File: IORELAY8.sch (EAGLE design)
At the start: 54 parts, among them J1 M08-SCREW-3.5MM, J2 M08-SCREW-3.5MM, J3 M10-PLAIN, J4 M06X2-SHROUDED, Q1 2N7002, Q2 2N7002, Q3 2N7002, Q4 2N7002, Q5 2N7002, Q6 2N7002, Q7 2N7002, Q8 2N7002

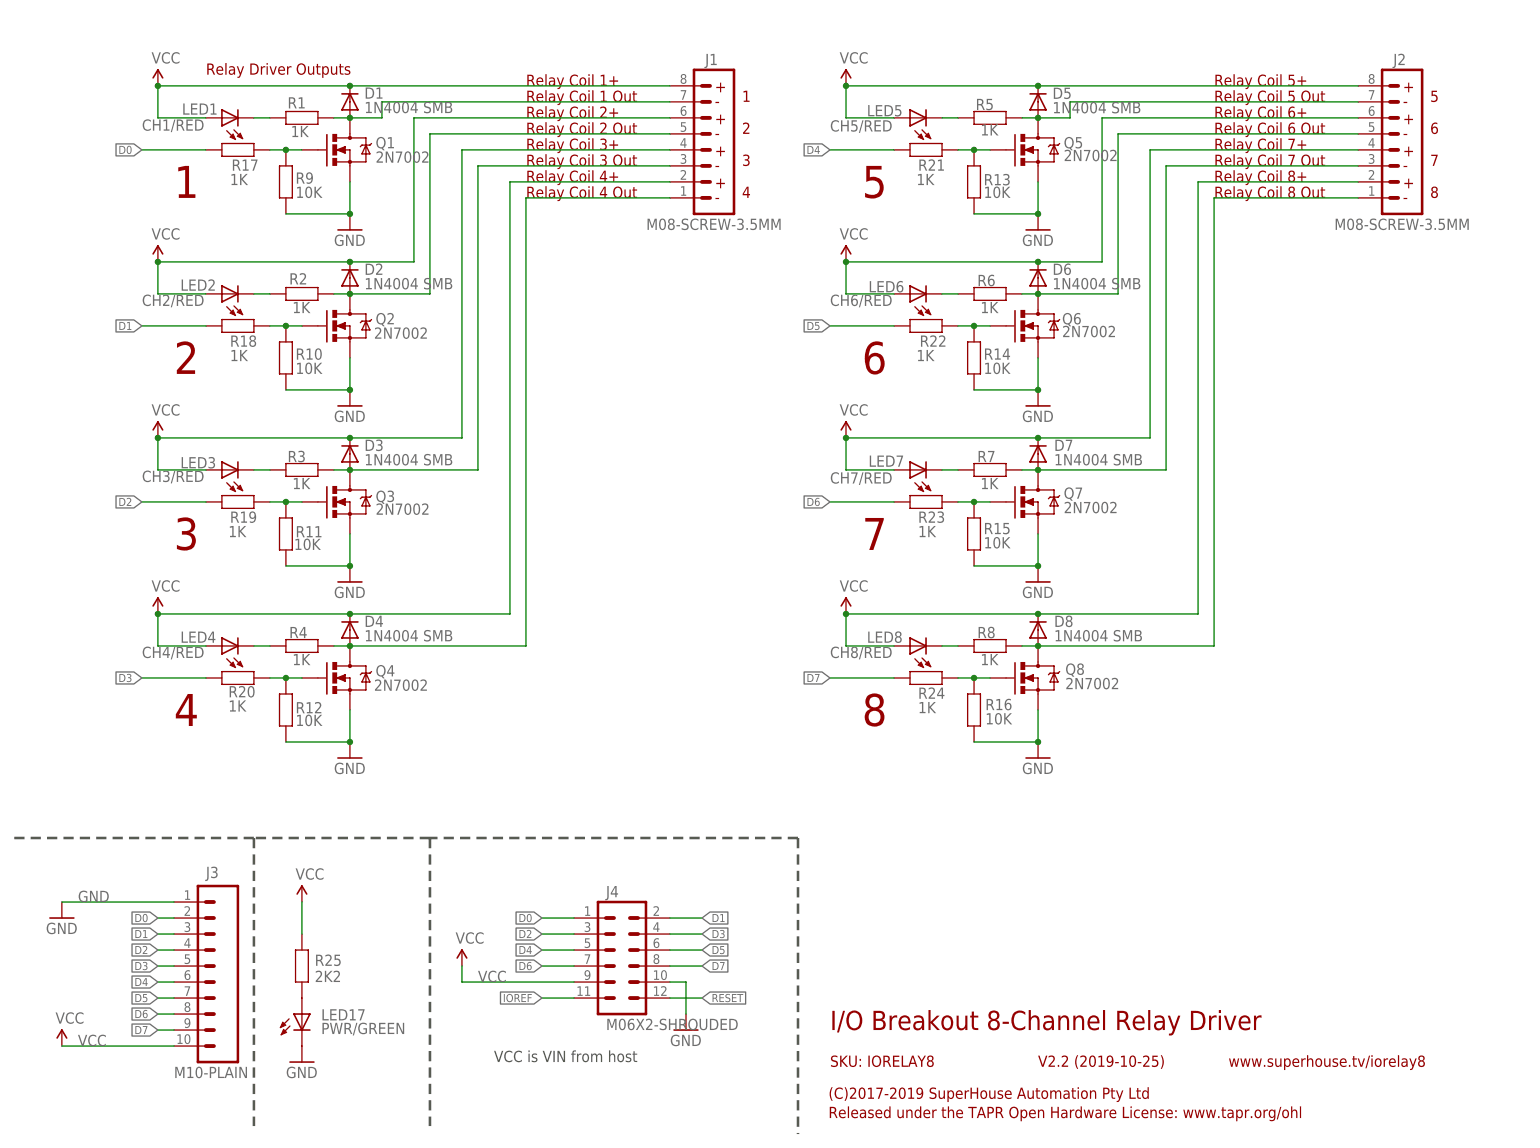
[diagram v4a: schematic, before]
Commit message: DRC, designator, and value cleanups for v2.2 release
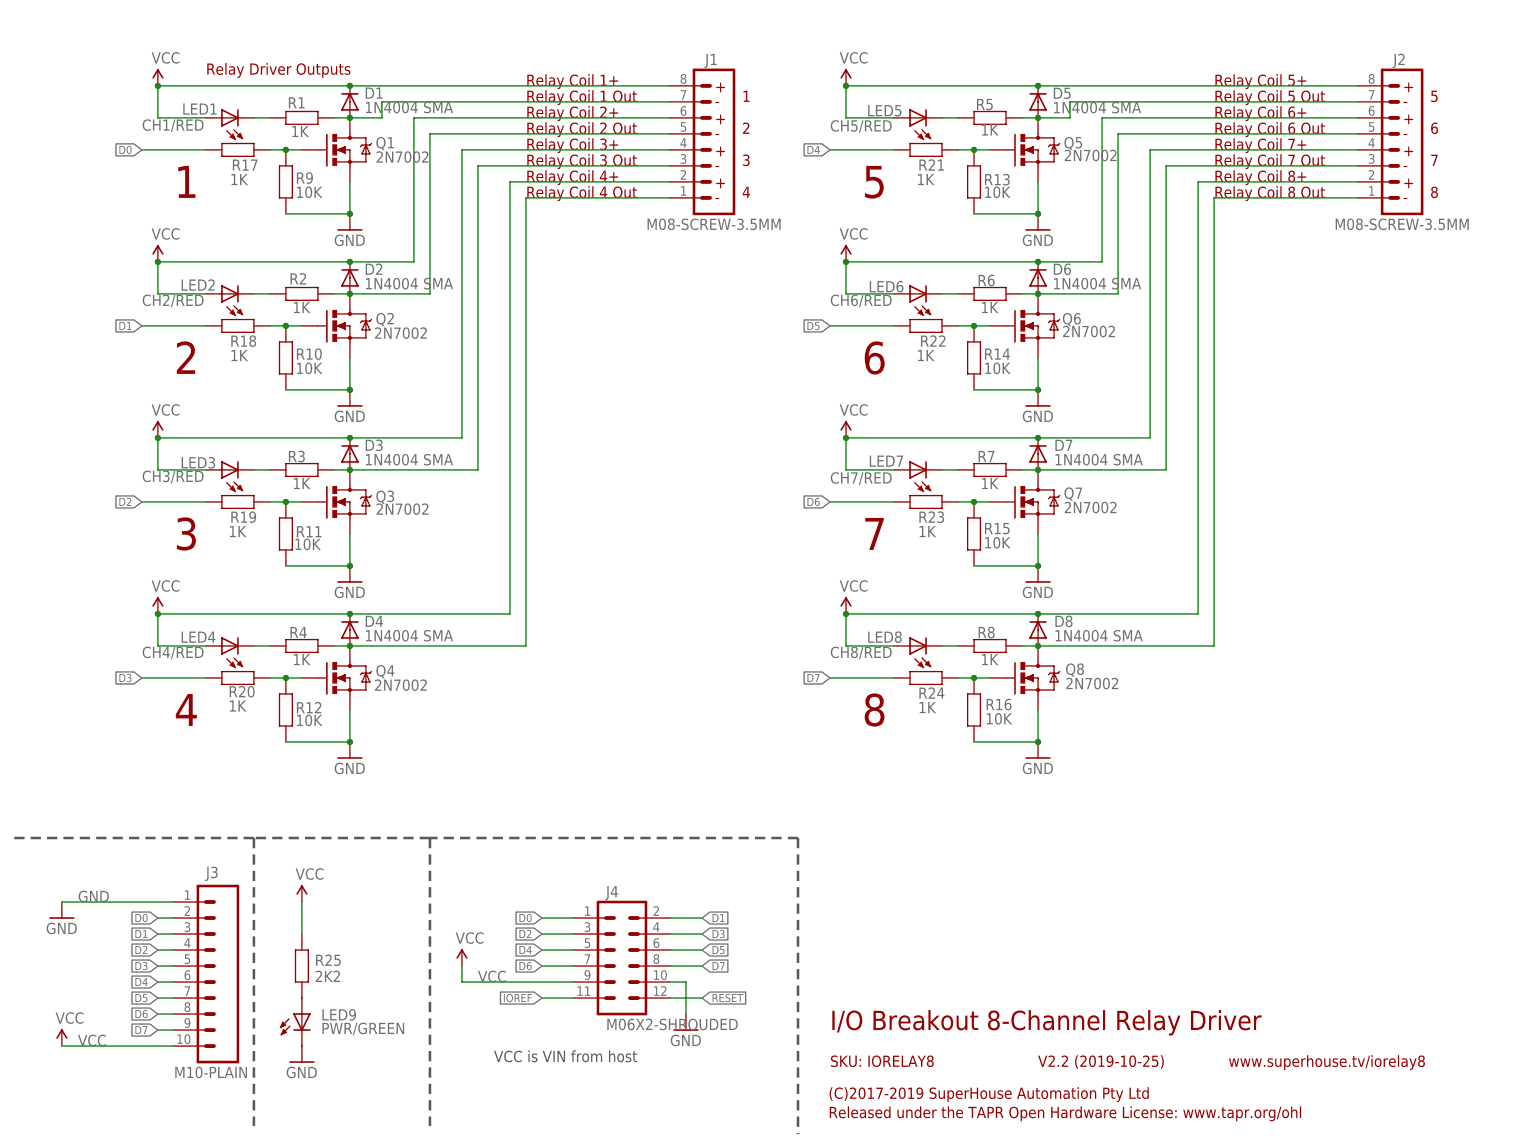
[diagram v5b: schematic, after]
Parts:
- D1, D2, D3, D4, D5, D6, D7, D8: value 1N4004 SMB -> 1N4004 SMA
- renumbered LED17 to LED9
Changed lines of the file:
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@@
 <part name="R7" library="SuperHouse-DiscreteSemi" library_urn="urn:adsk.eagle:library:11768461" deviceset="RESISTOR" device="0603" package3d_urn="urn:adsk.eagle:package:11768543/2" value="1K"/>
 <part name="R8" library="SuperHouse-DiscreteSemi" library_urn="urn:adsk.eagle:library:11768461" deviceset="RESISTOR" device="0603" package3d_urn="urn:adsk.eagle:package:11768543/2" value="1K"/>
-<part name="D1" library="SuperHouse-DiscreteSemi" library_urn="urn:adsk.eagle:library:11768461" deviceset="DIODE" device="SMA" package3d_urn="urn:adsk.eagle:package:7066222/3" value="1N4004 SMB"/>
-<part name="D2" library="SuperHouse-DiscreteSemi" library_urn="urn:adsk.eagle:library:11768461" deviceset="DIODE" device="SMA" package3d_urn="urn:adsk.eagle:package:7066222/3" value="1N4004 SMB"/>
-<part name="D3" library="SuperHouse-DiscreteSemi" library_urn="urn:adsk.eagle:library:11768461" deviceset="DIODE" device="SMA" package3d_urn="urn:adsk.eagle:package:7066222/3" value="1N4004 SMB"/>
-<part name="D4" library="SuperHouse-DiscreteSemi" library_urn="urn:adsk.eagle:library:11768461" deviceset="DIODE" device="SMA" package3d_urn="urn:adsk.eagle:package:7066222/3" value="1N4004 SMB"/>
-<part name="D5" library="SuperHouse-DiscreteSemi" library_urn="urn:adsk.eagle:library:11768461" deviceset="DIODE" device="SMA" package3d_urn="urn:adsk.eagle:package:7066222/3" value="1N4004 SMB"/>
-<part name="D6" library="SuperHouse-DiscreteSemi" library_urn="urn:adsk.eagle:library:11768461" deviceset="DIODE" device="SMA" package3d_urn="urn:adsk.eagle:package:7066222/3" value="1N4004 SMB"/>
-<part name="D7" library="SuperHouse-DiscreteSemi" library_urn="urn:adsk.eagle:library:11768461" deviceset="DIODE" device="SMA" package3d_urn="urn:adsk.eagle:package:7066222/3" value="1N4004 SMB"/>
-<part name="D8" library="SuperHouse-DiscreteSemi" library_urn="urn:adsk.eagle:library:11768461" deviceset="DIODE" device="SMA" package3d_urn="urn:adsk.eagle:package:7066222/3" value="1N4004 SMB"/>
-<part name="LED17" library="SuperHouse-LEDs" library_urn="urn:adsk.eagle:library:11790571" deviceset="LED" device="0603" package3d_urn="urn:adsk.eagle:package:7066240/3" value="PWR/GREEN"/>
+<part name="D1" library="SuperHouse-DiscreteSemi" library_urn="urn:adsk.eagle:library:11768461" deviceset="DIODE" device="SMA" package3d_urn="urn:adsk.eagle:package:7066222/3" value="1N4004 SMA"/>
+<part name="D2" library="SuperHouse-DiscreteSemi" library_urn="urn:adsk.eagle:library:11768461" deviceset="DIODE" device="SMA" package3d_urn="urn:adsk.eagle:package:7066222/3" value="1N4004 SMA"/>
+<part name="D3" library="SuperHouse-DiscreteSemi" library_urn="urn:adsk.eagle:library:11768461" deviceset="DIODE" device="SMA" package3d_urn="urn:adsk.eagle:package:7066222/3" value="1N4004 SMA"/>
+<part name="D4" library="SuperHouse-DiscreteSemi" library_urn="urn:adsk.eagle:library:11768461" deviceset="DIODE" device="SMA" package3d_urn="urn:adsk.eagle:package:7066222/3" value="1N4004 SMA"/>
+<part name="D5" library="SuperHouse-DiscreteSemi" library_urn="urn:adsk.eagle:library:11768461" deviceset="DIODE" device="SMA" package3d_urn="urn:adsk.eagle:package:7066222/3" value="1N4004 SMA"/>
+<part name="D6" library="SuperHouse-DiscreteSemi" library_urn="urn:adsk.eagle:library:11768461" deviceset="DIODE" device="SMA" package3d_urn="urn:adsk.eagle:package:7066222/3" value="1N4004 SMA"/>
+<part name="D7" library="SuperHouse-DiscreteSemi" library_urn="urn:adsk.eagle:library:11768461" deviceset="DIODE" device="SMA" package3d_urn="urn:adsk.eagle:package:7066222/3" value="1N4004 SMA"/>
+<part name="D8" library="SuperHouse-DiscreteSemi" library_urn="urn:adsk.eagle:library:11768461" deviceset="DIODE" device="SMA" package3d_urn="urn:adsk.eagle:package:7066222/3" value="1N4004 SMA"/>
+<part name="LED9" library="SuperHouse-LEDs" library_urn="urn:adsk.eagle:library:11790571" deviceset="LED" device="0603" package3d_urn="urn:adsk.eagle:package:7066240/3" value="PWR/GREEN"/>
 <part name="GND24" library="freetronics" deviceset="GND" device=""/>
 <part name="R25" library="SuperHouse-DiscreteSemi" library_urn="urn:adsk.eagle:library:11768461" deviceset="RESISTOR" device="0603" package3d_urn="urn:adsk.eagle:package:11768543/2" value="2K2"/>
@@
 <attribute name="VALUE" x="170.18" y="82.0166" size="1.778" layer="96"/>
 </instance>
-<instance part="LED17" gate="G$1" x="50.8" y="22.86" smashed="yes">
+<instance part="LED9" gate="G$1" x="50.8" y="22.86" smashed="yes">
 <attribute name="NAME" x="53.848" y="21.844" size="1.778" layer="95"/>
 <attribute name="VALUE" x="53.848" y="19.685" size="1.778" layer="96"/>
@@
 </segment>
 <segment>
-<pinref part="LED17" gate="G$1" pin="C"/>
+<pinref part="LED9" gate="G$1" pin="C"/>
 <pinref part="GND24" gate="1" pin="GND"/>
 </segment>
@@
 <net name="N$4" class="0">
 <segment>
-<pinref part="LED17" gate="G$1" pin="A"/>
+<pinref part="LED9" gate="G$1" pin="A"/>
 <pinref part="R25" gate="G$1" pin="1"/>
 </segment>
